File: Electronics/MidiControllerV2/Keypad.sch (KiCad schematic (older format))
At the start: 0 parts

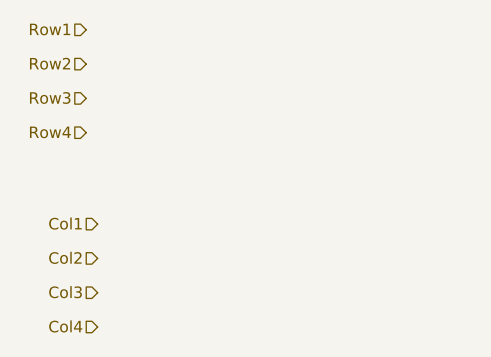
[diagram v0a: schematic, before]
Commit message: #32 Pcb v2 components placed
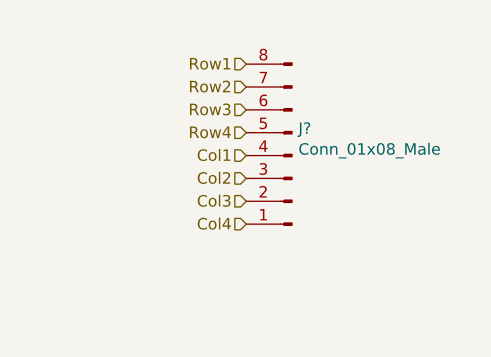
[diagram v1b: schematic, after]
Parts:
- added J?: Conn_01x08_Male, symbol Connector:Conn_01x08_Male
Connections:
- net Col1: now also J?.4 (Pin_4)
- net Col2: now also J?.3 (Pin_3)
- net Col3: now also J?.2 (Pin_2)
- net Col4: now also J?.1 (Pin_1)
- net Row1: now also J?.8 (Pin_8)
- net Row2: now also J?.7 (Pin_7)
- net Row3: now also J?.6 (Pin_6)
- net Row4: now also J?.5 (Pin_5)
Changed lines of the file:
@@
 Comment4 ""
 $EndDescr
-Text HLabel 3250 2450 0    50   Input ~ 0
+Text HLabel 3950 2600 0    50   Input ~ 0
 Row1
-Text HLabel 3250 2600 0    50   Input ~ 0
+Text HLabel 3950 2700 0    50   Input ~ 0
 Row2
-Text HLabel 3250 2750 0    50   Input ~ 0
+Text HLabel 3950 2800 0    50   Input ~ 0
 Row3
-Text HLabel 3250 2900 0    50   Input ~ 0
+Text HLabel 3950 2900 0    50   Input ~ 0
 Row4
-Text HLabel 3300 3300 0    50   Input ~ 0
+Text HLabel 3950 3000 0    50   Input ~ 0
 Col1
-Text HLabel 3300 3450 0    50   Input ~ 0
+Text HLabel 3950 3100 0    50   Input ~ 0
 Col2
-Text HLabel 3300 3600 0    50   Input ~ 0
+Text HLabel 3950 3200 0    50   Input ~ 0
 Col3
-Text HLabel 3300 3750 0    50   Input ~ 0
+Text HLabel 3950 3300 0    50   Input ~ 0
 Col4
+$Comp
+L Connector:Conn_01x08_Male J?
+U 1 1 5FFC38A0
+P 4150 3000
+F 0 "J?" H 4122 2882 50  0000 R CNN
+F 1 "Conn_01x08_Male" H 4122 2973 50  0000 R CNN
+F 2 "" H 4150 3000 50  0001 C CNN
+F 3 "~" H 4150 3000 50  0001 C CNN
+	1    4150 3000
+	-1   0    0    1
+$EndComp
 $EndSCHEMATC
